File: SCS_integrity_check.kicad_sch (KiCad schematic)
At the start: 18 parts, among them U18 LM393ADGKR, U19 OPA355NA, U20 OPA355NA, U21 OPA355NA, U22 LM393ADGKR, U23 LM393ADGKR

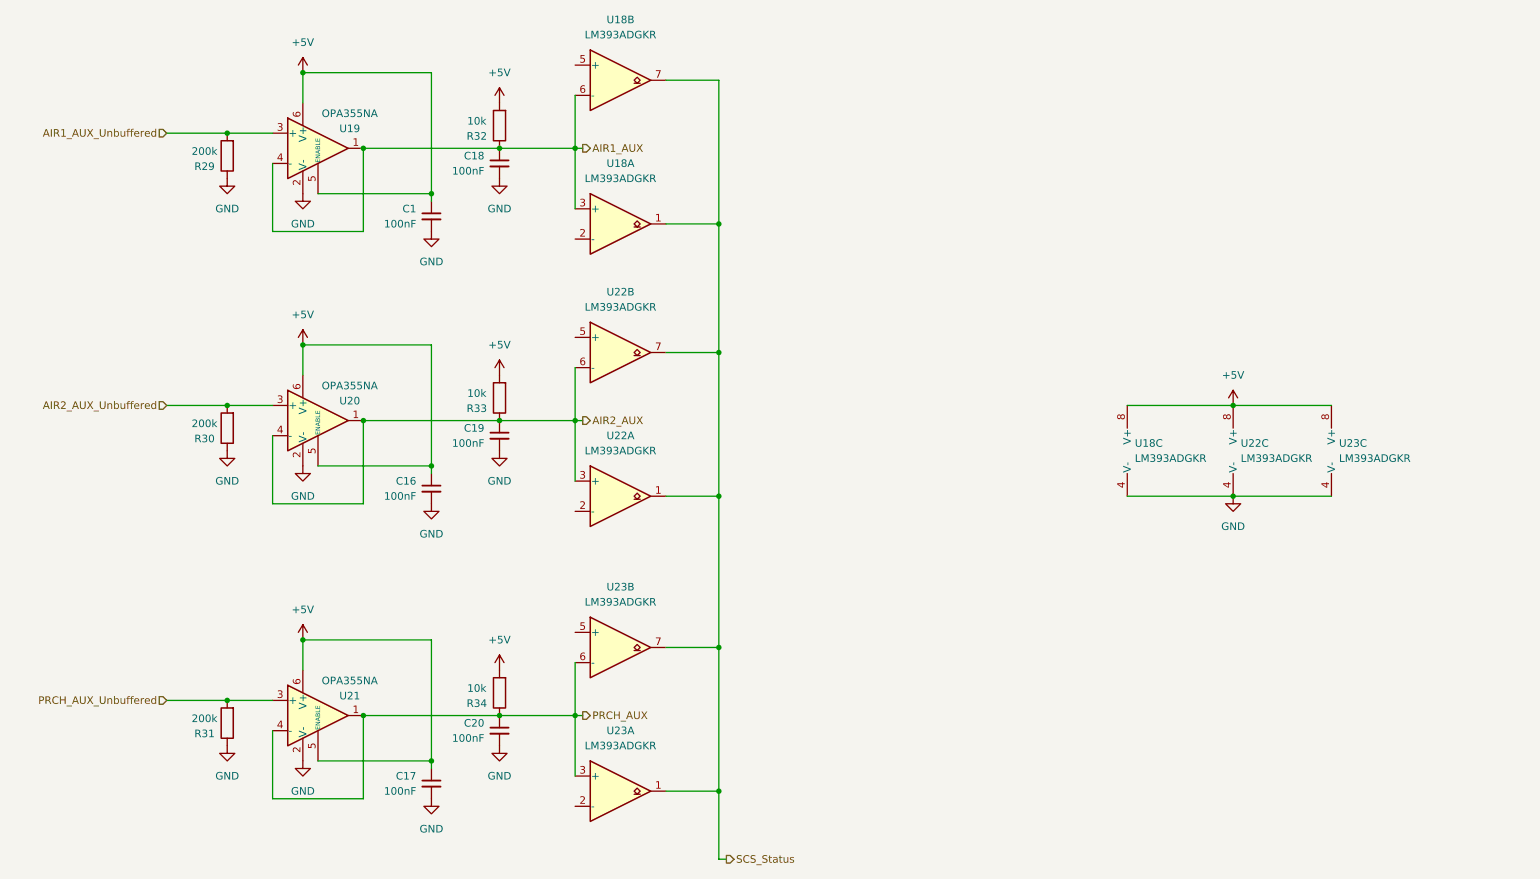
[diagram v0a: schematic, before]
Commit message: Added decoupling Caps
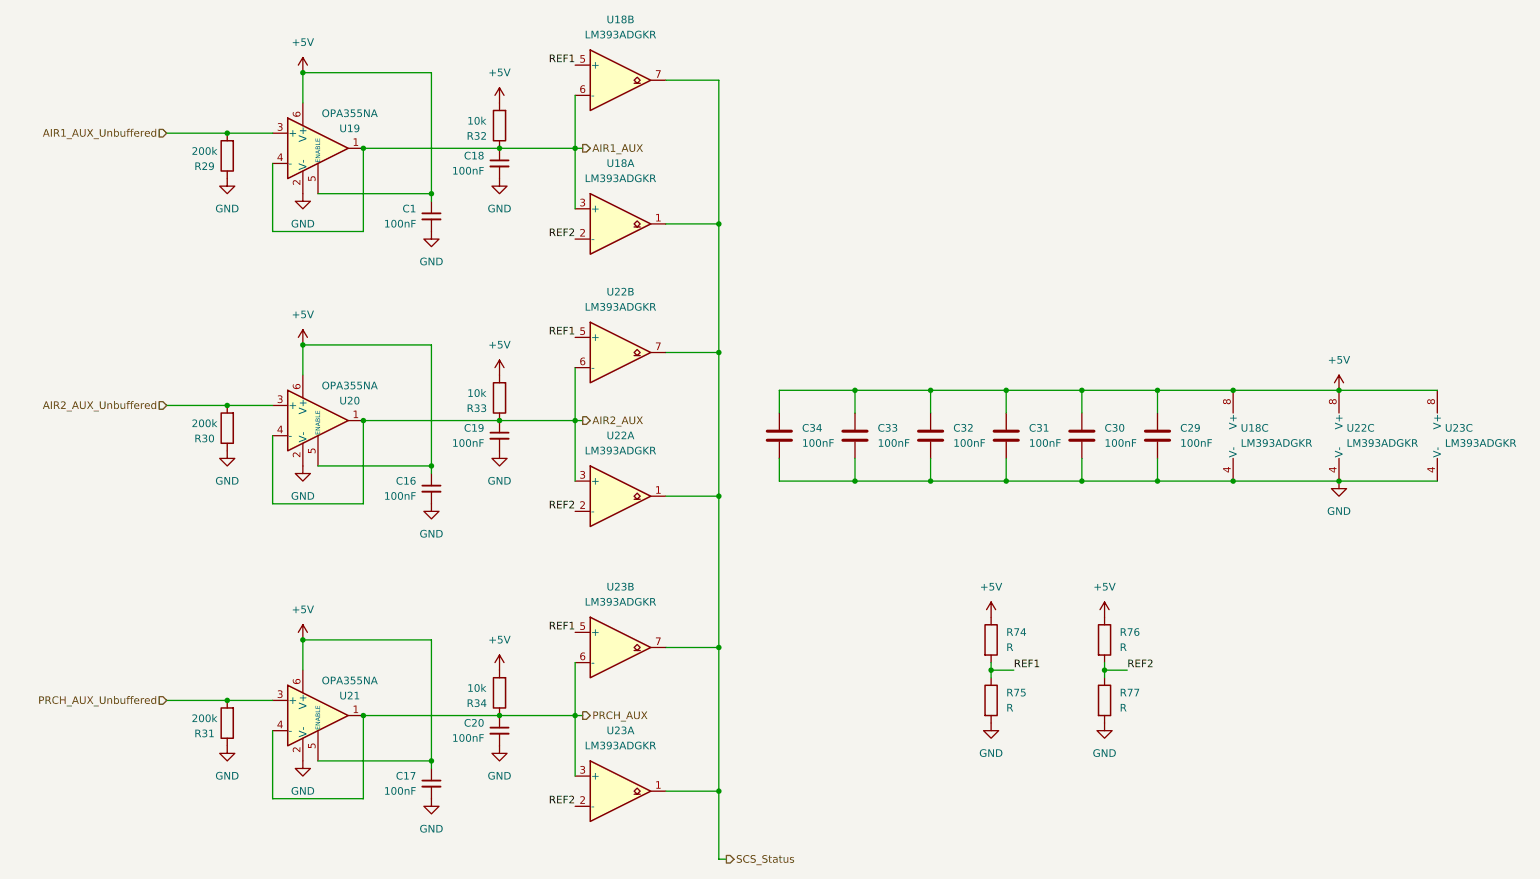
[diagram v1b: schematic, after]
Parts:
- added C29, C30, C31, C32, C33, C34: 100nF, symbol Device:C
- added R74, R75, R76, R77: R, symbol Device:R
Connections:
- net +5V: now also C29.1, C30.1, C31.1, C32.1, C33.1, C34.1, R74.1, R76.1
- net GND: now also C29.2, C30.2, C31.2, C32.2, C33.2, C34.2, R75.2, R77.2
- net REF2: now reaches U22.2 (-)
- net REF2: now also U18.2 (-), U23.2 (-), R76.2, R77.1
- net REF1: now reaches U23.5 (+)
- net REF1: now also U18.5 (+), U22.5 (+), R74.2, R75.1
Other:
- moved on the sheet: U18C, U22C, U23C
